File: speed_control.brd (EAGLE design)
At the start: 31.7 x 23.8 mm, 9 parts

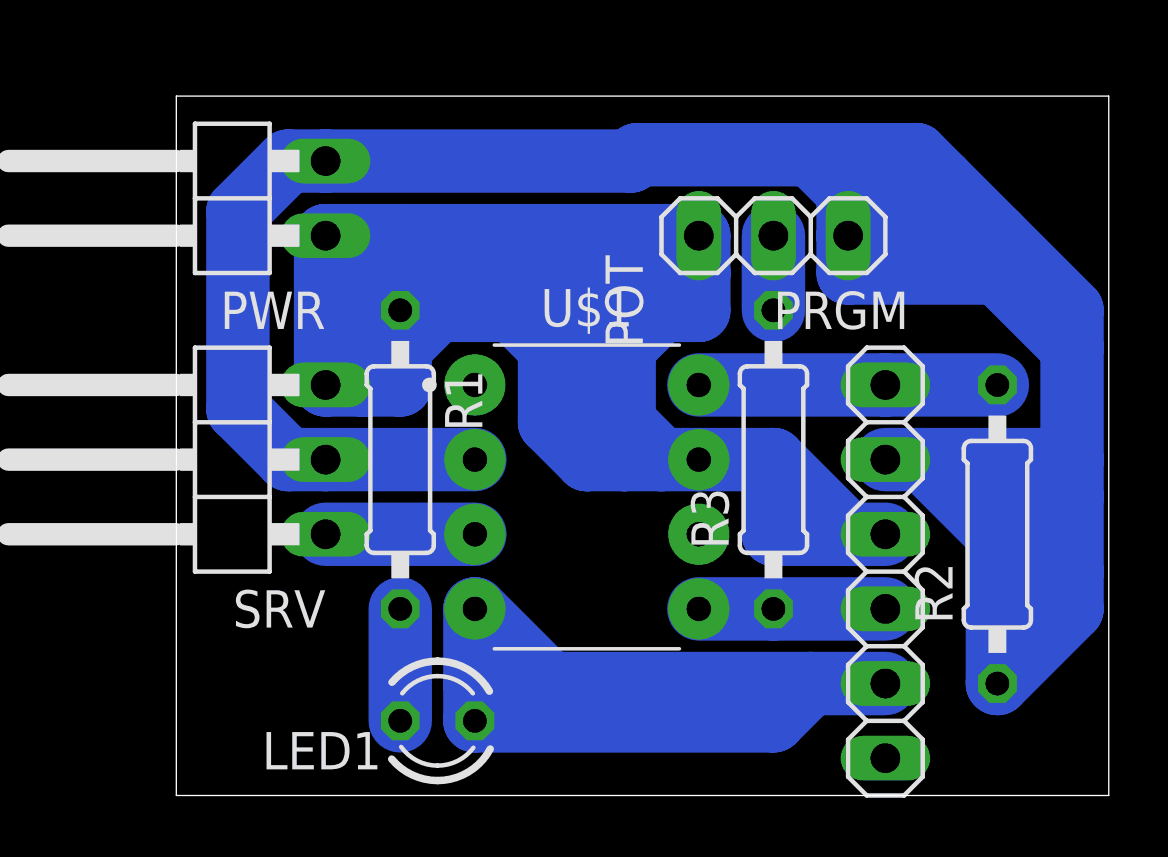
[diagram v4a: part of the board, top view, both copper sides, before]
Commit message: Added CAP to circuit
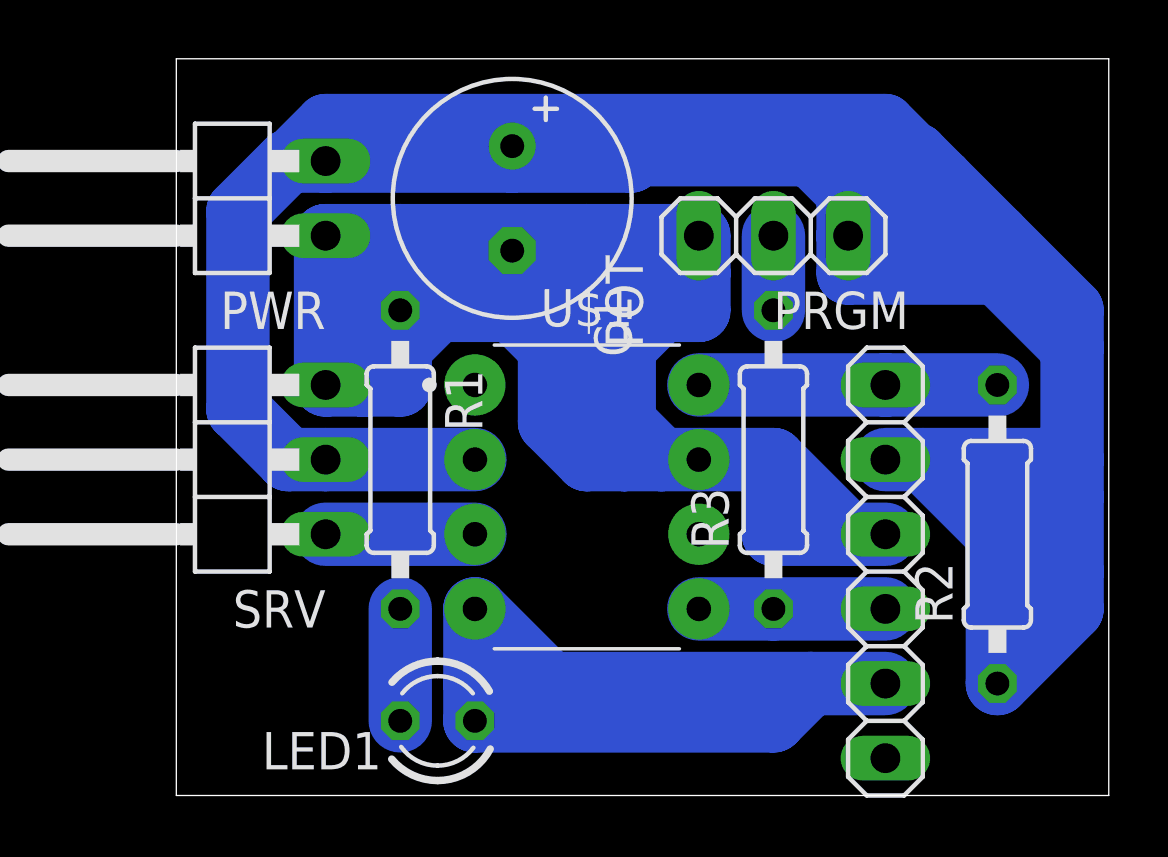
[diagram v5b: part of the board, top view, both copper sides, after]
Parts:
- added C1: (no value), rcl:E3,5-8
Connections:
- net 5V: now also C1.+
- net GND: now also C1.-
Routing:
- net 5V: track 109.8 -> 133.8 mm
- net GND: track 93.6 -> 95.1 mm
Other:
- board size 31.7 x 23.8 mm -> 31.7 x 25.1 mm
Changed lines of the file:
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@@
 <plain>
 <wire x1="0" y1="0" x2="31.73" y2="0" width="0" layer="20"/>
-<wire x1="31.73" y1="0" x2="31.73" y2="23.8" width="0" layer="20"/>
-<wire x1="31.73" y1="23.8" x2="0" y2="23.8" width="0" layer="20"/>
-<wire x1="0" y1="23.8" x2="0" y2="0" width="0" layer="20"/>
+<wire x1="31.73" y1="0" x2="31.73" y2="25.07" width="0" layer="20"/>
+<wire x1="31.73" y1="25.07" x2="0" y2="25.07" width="0" layer="20"/>
+<wire x1="0" y1="25.07" x2="0" y2="0" width="0" layer="20"/>
 </plain>
 <attributes>
@@
 <attribute name="VALUE" x="26.035" y="15.24" size="1.27" layer="27" rot="R90"/>
 </element>
+<element name="C1" library="rcl" library_urn="urn:adsk.eagle:library:334" package="E3,5-8" package3d_urn="urn:adsk.eagle:package:23360/2" value="" x="11.43" y="20.32" smashed="yes" rot="R270">
+<attribute name="NAME" x="14.224" y="17.018" size="1.27" layer="25" ratio="10" rot="R270"/>
+<attribute name="POPULARITY" value="13" x="11.43" y="20.32" size="1.778" layer="27" rot="R270" display="off"/>
+<attribute name="SPICEPREFIX" value="C" x="11.43" y="20.32" size="1.778" layer="27" rot="R270" display="off"/>
+<attribute name="VALUE" x="8.382" y="22.606" size="1.27" layer="27" ratio="10" rot="R270"/>
+</element>
 </elements>
 <signals>
@@
 <wire x1="13.97" y1="11.43" x2="13.97" y2="16.51" width="2.159" layer="16"/>
 <wire x1="13.97" y1="19.05" x2="13.97" y2="16.51" width="2.159" layer="16"/>
-<wire x1="13.97" y1="19.05" x2="7.62" y2="19.05" width="2.159" layer="16"/>
+<wire x1="13.97" y1="19.05" x2="10.16" y2="19.05" width="2.159" layer="16"/>
+<wire x1="10.16" y1="19.05" x2="7.62" y2="19.05" width="2.159" layer="16"/>
 <wire x1="7.62" y1="19.05" x2="5.08" y2="19.05" width="2.159" layer="16"/>
 <wire x1="17.78" y1="19.05" x2="13.97" y2="19.05" width="2.159" layer="16"/>
@@
 <wire x1="16.51" y1="16.51" x2="15.24" y2="15.24" width="2.159" layer="16"/>
 <wire x1="16.51" y1="11.43" x2="15.24" y2="12.7" width="2.159" layer="16"/>
+<contactref element="C1" pad="-"/>
+<wire x1="11.43" y1="18.542" x2="10.668" y2="18.542" width="2.032" layer="16"/>
+<wire x1="10.668" y1="18.542" x2="10.16" y2="19.05" width="2.032" layer="16"/>
 </signal>
 <signal name="5V">
@@
 <wire x1="27.94" y1="11.43" x2="25.4" y2="11.43" width="2.159" layer="16"/>
 <wire x1="25.4" y1="11.43" x2="24.13" y2="11.43" width="2.159" layer="16"/>
-<wire x1="5.08" y1="21.59" x2="15.46819375" y2="21.59" width="2.159" layer="16"/>
+<wire x1="5.08" y1="21.59" x2="11.43" y2="21.59" width="2.159" layer="16"/>
+<wire x1="11.43" y1="21.59" x2="15.46819375" y2="21.59" width="2.159" layer="16"/>
 <wire x1="15.46819375" y1="21.59" x2="15.68409375" y2="21.8059" width="2.159" layer="16"/>
 <wire x1="15.68409375" y1="21.8059" x2="21.59" y2="21.8059" width="2.159" layer="16"/>
@@
 <wire x1="24.13" y1="20.7518" x2="24.13" y2="19.05" width="2.159" layer="16"/>
 <wire x1="26.035" y1="20.955" x2="25.4" y2="20.32" width="2.159" layer="16"/>
+<contactref element="C1" pad="+"/>
+<wire x1="3.81" y1="21.59" x2="5.08" y2="22.86" width="2.032" layer="16"/>
+<wire x1="5.08" y1="22.86" x2="24.13" y2="22.86" width="2.032" layer="16"/>
+<wire x1="24.13" y1="22.86" x2="26.035" y2="20.955" width="2.032" layer="16"/>
+<wire x1="11.43" y1="22.098" x2="11.43" y2="21.59" width="2.032" layer="16"/>
 </signal>
 <signal name="SIGNAL">

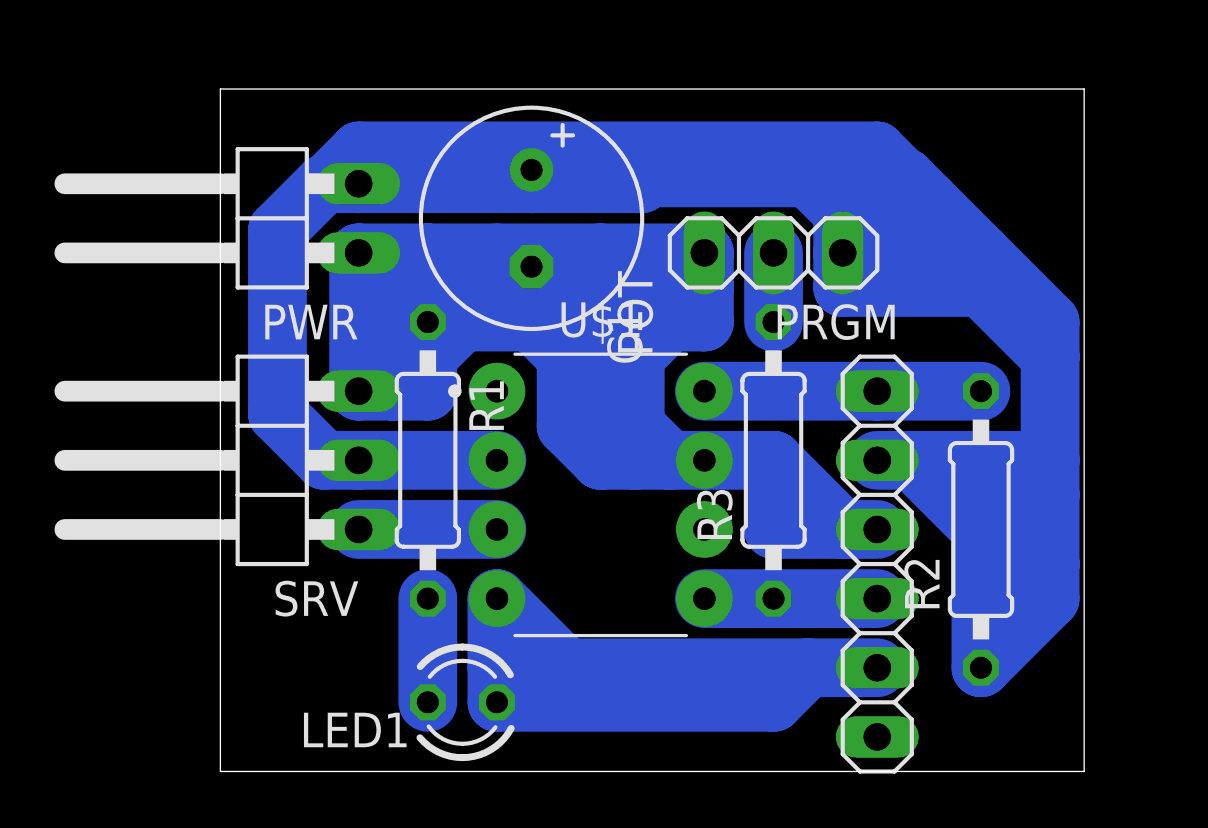
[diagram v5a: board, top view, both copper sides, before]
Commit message: Added mounting holes
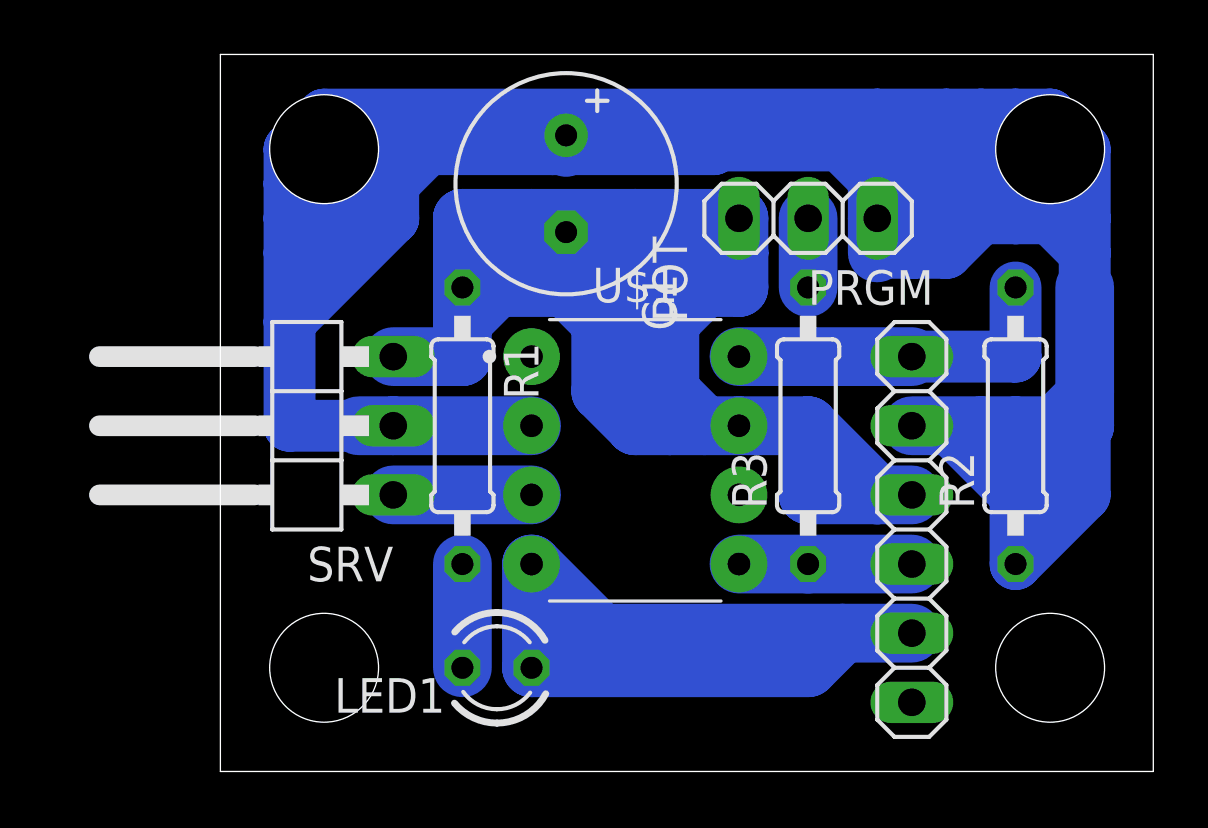
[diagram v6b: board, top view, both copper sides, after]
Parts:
- removed PWR: (no value), pinhead:1X02/90
- moved R2 4.02 mm to (29.2, 12.7)
- moved LED1 1.80 mm to (10.2, 3.81)
- moved PRGM 1.80 mm to (25.4, 8.89)
- moved R1 1.80 mm to (8.89, 12.7)
- moved SRV 1.80 mm to (2.54, 12.7)
- moved C1 1.80 mm to (12.7, 21.6)
- moved POT 1.80 mm to (21.6, 20.3)
- moved R3 1.80 mm to (21.6, 12.7)
- moved U$1 1.80 mm to (15.2, 11.4)
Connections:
- net 5V: no longer PWR.2
- net GND: no longer PWR.1
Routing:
- net 5V: track 133.8 -> 167.2 mm
- net GND: track 95.1 -> 81.9 mm
- net MCLR/VPP: track 10.2 -> 12.7 mm
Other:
- board size 31.7 x 25.1 mm -> 34.3 x 26.3 mm
